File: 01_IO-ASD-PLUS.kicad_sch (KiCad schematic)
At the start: 0 parts

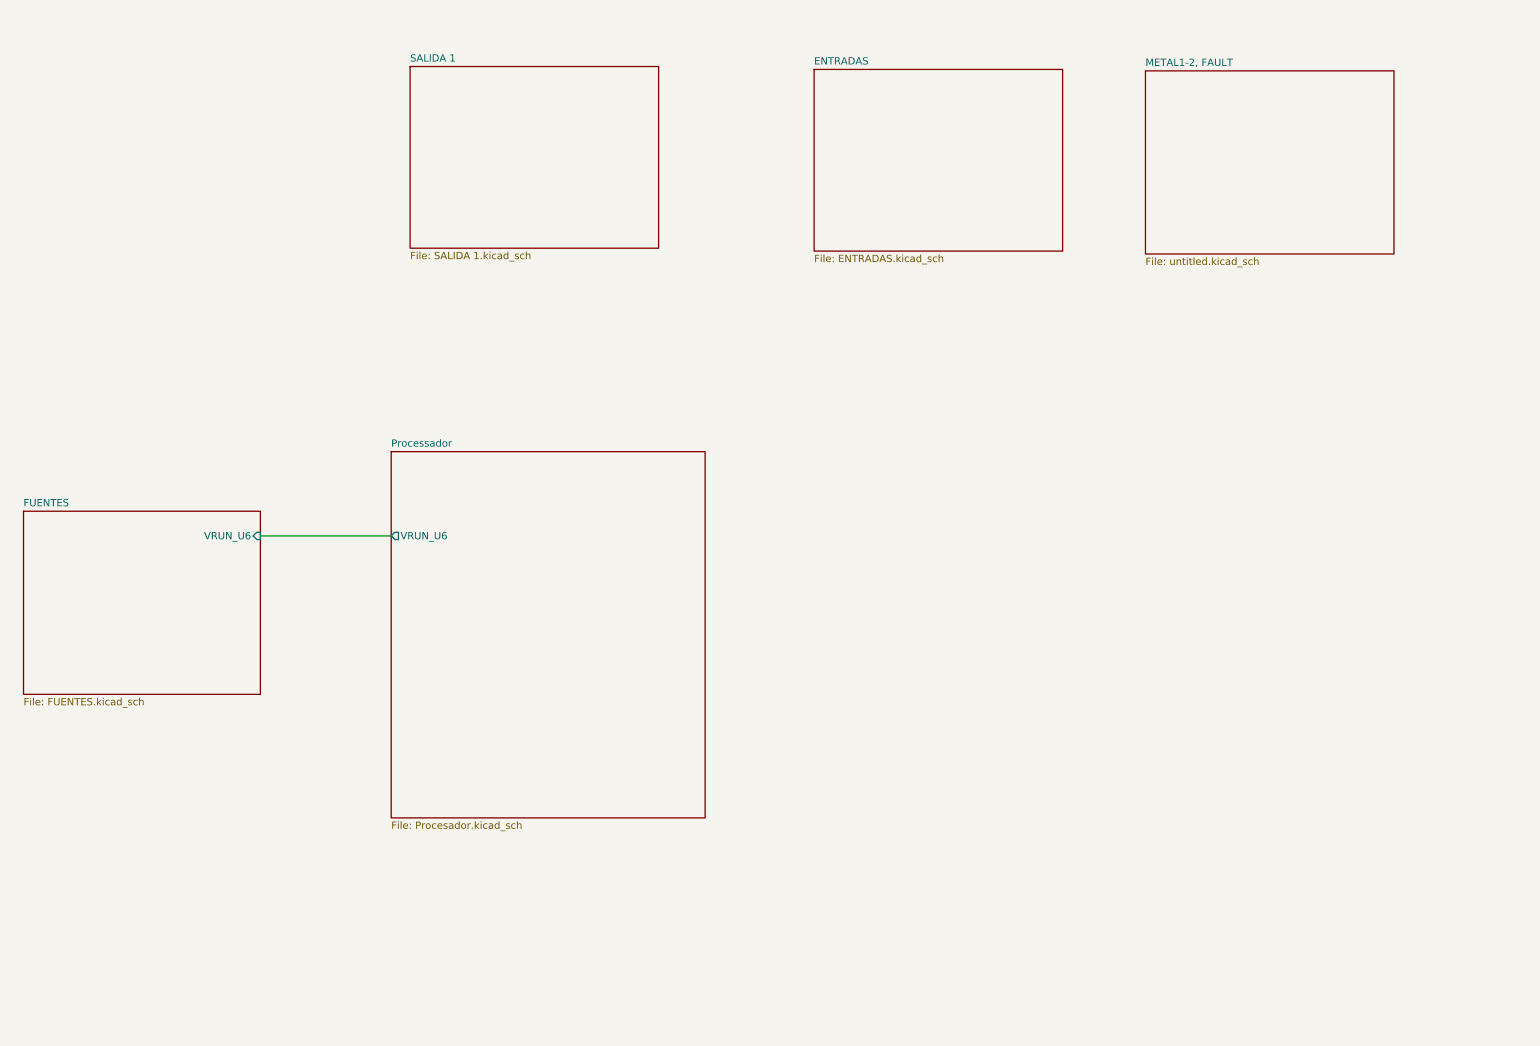
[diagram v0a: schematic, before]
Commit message: 13-Mayo26 se agrego hoja de procesador y USB
hoja de USB AL 95% HOJA DEL procesador al 75%
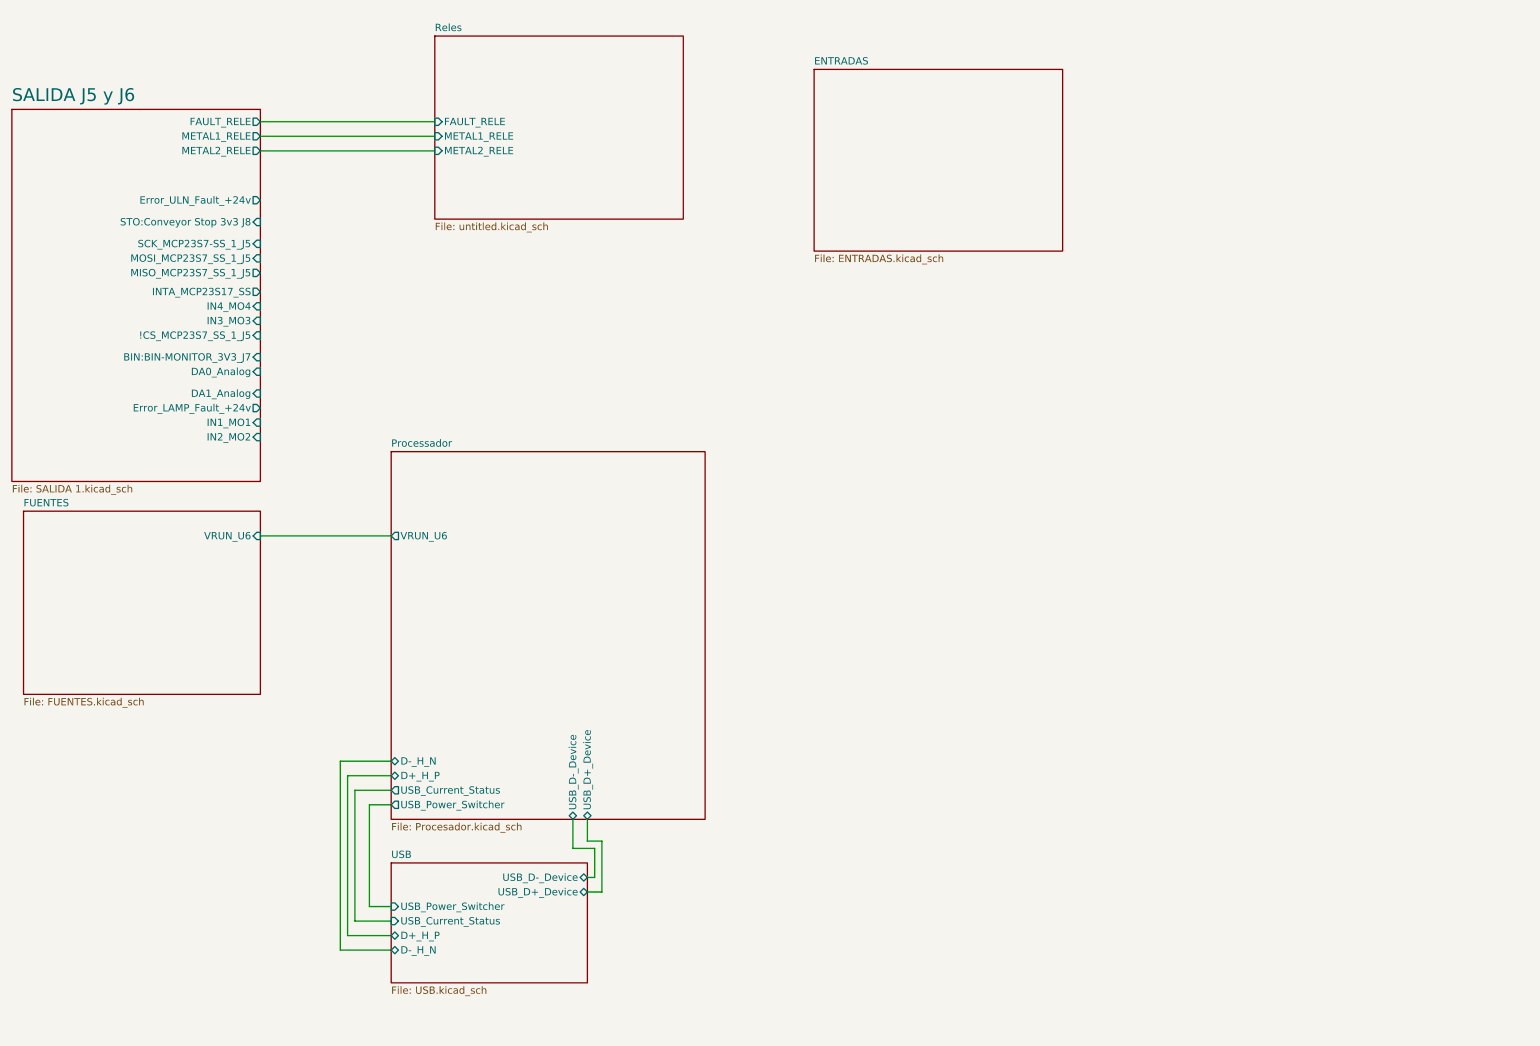
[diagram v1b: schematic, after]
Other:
- sheet METAL1-2, FAULT renamed Reles
- sheet SALIDA 1 renamed SALIDA J5 y J6
- added sheet USB (USB.kicad_sch)
- sheet Processador ports: added D+_H_P, D-_H_N, USB_Current_Status, USB_D+_Device, USB_D-_Device, USB_Power_Switcher; removed none
- sheet Reles ports: added FAULT_RELE, METAL1_RELE, METAL2_RELE; removed none
- sheet SALIDA J5 y J6 ports: added !CS_MCP23S7_SS_1_J5, BIN:BIN-MONITOR_3V3_J7, DA0_Analog, DA1_Analog, Error_LAMP_Fault_+24v, Error_ULN_Fault_+24v, FAULT_RELE, IN1_MO1, IN2_MO2, IN3_MO3, IN4_MO4, INTA_MCP23S17_SS, METAL1_RELE, METAL2_RELE, MISO_MCP23S7_SS_1_J5, MOSI_MCP23S7_SS_1_J5, SCK_MCP23S7-SS_1_J5, STO:Conveyor Stop 3v3 J8; removed none

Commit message: 14-Mayo-26
se agregaron varias sheet de esquematico crecio al 80% la parte de esquematico
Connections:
- no-connect marks 0 -> 2
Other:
- added sheet ENTRADAS1 (ENTRADAS.kicad_sch)
- added sheet ENTRADAS2 (ENTRADAS.kicad_sch)
- added sheet Ent Especial (Entrada Especial.kicad_sch)
- added sheet Port Expansor (Port_Expansor.kicad_sch)
- added sheet Serial_Comm (Comm_Serial.kicad_sch)
- sheet ENTRADAS ports: added opto_out1, opto_out2, opto_out3, opto_out4, opto_out5, opto_out6; removed none
